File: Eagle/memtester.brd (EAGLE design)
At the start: 69 x 22.3 mm, 15 parts, among them IC1 HT7833, J3 SM08B-SRSS-TB(LF)(SN), U1 ATTINY1616-MFR

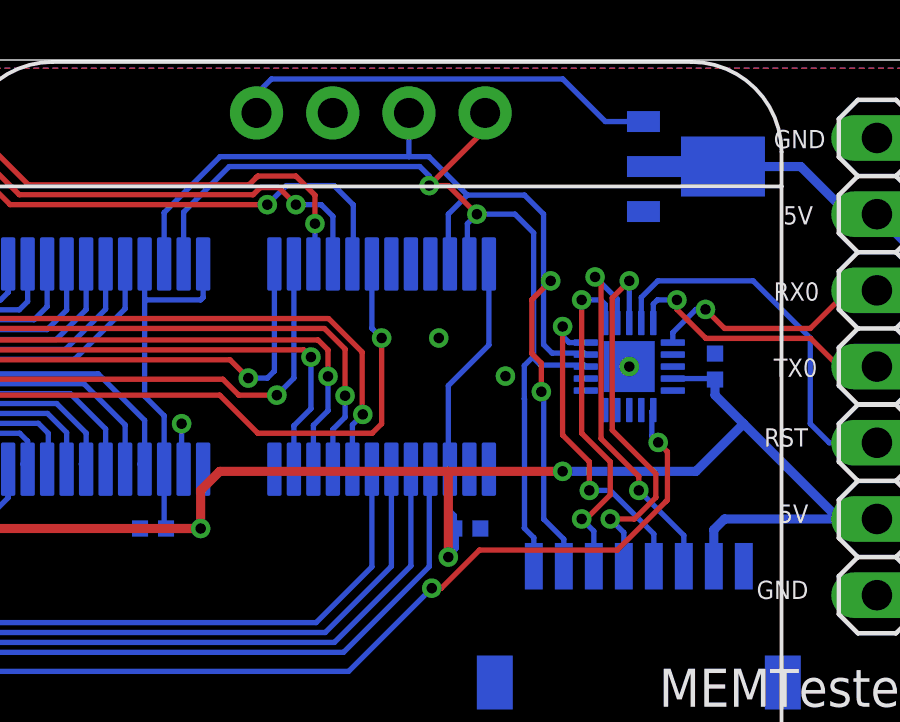
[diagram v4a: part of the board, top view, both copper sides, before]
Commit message: Memtester: i2c pull-ups, labels, credits
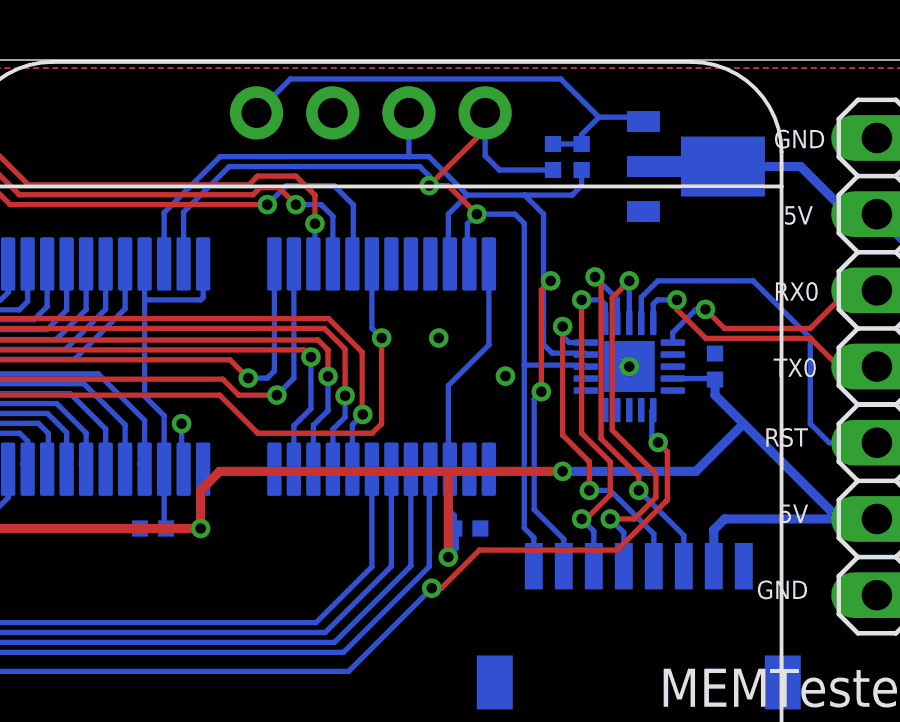
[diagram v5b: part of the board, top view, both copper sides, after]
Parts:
- added R1, R2: 4k7, passives:0402_RES
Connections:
- removed net N$1: IC1.1, U$6.VCC
- new net +3V3: IC1.1, R1.1, R2.1, U$6.VCC
- net I2C_SCL: now also R2.2
- net I2C_SDA: now also R1.2
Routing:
- net +3V3: track 0.00 -> 16.2 mm
- net N$1: track 14.3 -> 0.00 mm
- net I2C_SDA: track 33.4 -> 37.2 mm
- net I2C_SCL: track 36.4 -> 38.8 mm
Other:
- board text added: "Petrkr.NET"
- board text added: "Version 1 (2023/05)"
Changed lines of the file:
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@@
 <drawing>
 <settings>
-<setting alwaysvectorfont="yes"/>
+<setting alwaysvectorfont="no"/>
 <setting verticaltext="up"/>
 </settings>
@@
 <text x="60.96" y="6.985" size="0.6096" layer="26" rot="MR270" align="center-right">5V</text>
 <text x="61.9125" y="6.985" size="0.6096" layer="26" rot="MR270" align="center-right">GND</text>
+<text x="51.1175" y="0.635" size="0.8128" layer="26" rot="MR0">Version 1 (2023/05)</text>
+<text x="51.1175" y="2.2225" size="1.0668" layer="26" rot="MR0">Petrkr.NET</text>
 </plain>
 <attributes>
@@
 <element name="IC1" library="holtek2" package="SOT-89" value="HT7833" x="60.96" y="18.7325" smashed="yes" rot="MR90">
 <attribute name="LCSC_PART" value="C50936" x="69.85" y="11.1125" size="1.778" layer="28" rot="MR90" display="off"/>
-<attribute name="NAME" x="55.795" y="17.7975" size="1.27" layer="26" rot="MR90"/>
+<attribute name="NAME" x="61.8275" y="14.94" size="1.27" layer="26" rot="MR0"/>
 </element>
 <element name="C4" library="passives" package="0402_CAP" value="100nF" x="60.96" y="12.065" smashed="yes" rot="MR90">
-<attribute name="NAME" x="59.436" y="12.065" size="0.635" layer="26" font="vector" ratio="12" rot="MR90" align="bottom-center"/>
+<attribute name="NAME" x="60.706" y="10.4775" size="0.635" layer="26" font="vector" ratio="12" rot="MR90" align="bottom-center"/>
+</element>
+<element name="R2" library="passives" package="0402_RES" value="4k7" x="56.515" y="19.05" smashed="yes" rot="MR270">
+<attribute name="NAME" x="56.769" y="20.6375" size="0.635" layer="26" font="vector" ratio="12" rot="MR270" align="bottom-center"/>
+</element>
+<element name="R1" library="passives" package="0402_RES" value="4k7" x="55.5625" y="19.05" smashed="yes" rot="MR270">
+<attribute name="NAME" x="55.8165" y="20.6375" size="0.635" layer="26" font="vector" ratio="12" rot="MR270" align="bottom-center"/>
 </element>
 </elements>
@@
 <contactref element="U1" pad="13"/>
 <wire x1="56.6525" y1="12.065" x2="56.6038" y2="12.1137" width="0.1778" layer="16"/>
-<wire x1="56.6038" y1="12.1137" x2="55.1441875" y2="12.1137" width="0.1778" layer="16"/>
+<wire x1="56.6038" y1="12.1137" x2="54.61813125" y2="12.1137" width="0.1778" layer="16"/>
 <wire x1="52.705" y1="15.5525" x2="52.705" y2="16.8275" width="0.1778" layer="16"/>
 <wire x1="52.705" y1="15.5525" x2="52.7725" y2="15.485" width="0.1778" layer="16"/>
@@
 <wire x1="52.07" y1="18.0975" x2="51.435" y2="18.0975" width="0.1778" layer="1"/>
 <via x="53.0225" y="17.145" extent="1-16" drill="0.35"/>
-<wire x1="54.9148" y1="16.5227" x2="54.2925" y2="17.145" width="0.1778" layer="16"/>
+<wire x1="54.6025" y1="16.835" x2="54.2925" y2="17.145" width="0.1778" layer="16"/>
 <wire x1="53.0225" y1="17.145" x2="54.2925" y2="17.145" width="0.1778" layer="16"/>
-<wire x1="54.9148" y1="16.5227" x2="54.9148" y2="12.41036875" width="0.1778" layer="16"/>
+<wire x1="54.6025" y1="16.835" x2="54.6025" y2="12.09806875" width="0.1778" layer="16"/>
 <wire x1="52.705" y1="16.8275" x2="53.0225" y2="17.145" width="0.1778" layer="16"/>
 <contactref element="U$6" pad="SDA"/>
@@
 <wire x1="54.92" y1="5.41" x2="54.92" y2="6.3625" width="0.1778" layer="16"/>
 <wire x1="54.6025" y1="6.68" x2="54.92" y2="6.3625" width="0.1778" layer="16"/>
-<wire x1="54.9148" y1="12.41036875" x2="54.6025" y2="12.09806875" width="0.1778" layer="16"/>
-<wire x1="54.6025" y1="12.09806875" x2="54.6025" y2="10.99193125" width="0.1778" layer="16"/>
-<wire x1="54.6025" y1="10.99193125" x2="54.61" y2="10.98443125" width="0.1778" layer="16"/>
-<wire x1="54.61" y1="6.6875" x2="54.6025" y2="6.68" width="0.1778" layer="16"/>
-<wire x1="54.61" y1="10.98443125" x2="54.61" y2="6.6875" width="0.1778" layer="16"/>
-<wire x1="54.9148" y1="12.3430875" x2="54.9148" y2="12.41036875" width="0.1778" layer="16"/>
-<wire x1="55.1441875" y1="12.1137" x2="54.9148" y2="12.3430875" width="0.1778" layer="16"/>
+<wire x1="54.61813125" y1="12.1137" x2="54.6025" y2="12.09806875" width="0.1778" layer="16"/>
+<wire x1="54.6025" y1="12.09806875" x2="54.6025" y2="6.68" width="0.1778" layer="16"/>
+<contactref element="R1" pad="2"/>
+<wire x1="55.5625" y1="18.61693125" x2="53.77306875" y2="18.61693125" width="0.1778" layer="16"/>
+<wire x1="53.2975" y1="19.0925" x2="53.2975" y2="20.52" width="0.1778" layer="16"/>
+<wire x1="53.77306875" y1="18.61693125" x2="53.2975" y2="19.0925" width="0.1778" layer="16"/>
 </signal>
 <signal name="I2C_SCL">
@@
 <contactref element="J3" pad="7"/>
 <wire x1="55.92" y1="5.41" x2="55.92" y2="6.31" width="0.1778" layer="16"/>
-<wire x1="55.2502" y1="6.9798" x2="55.2502" y2="11.2275" width="0.1778" layer="16"/>
-<wire x1="55.2502" y1="11.2275" x2="55.1712" y2="11.2275" width="0.1778" layer="16"/>
+<wire x1="55.1712" y1="11.2275" x2="54.9327" y2="10.989" width="0.1778" layer="16"/>
+<wire x1="54.9327" y1="10.989" x2="54.9327" y2="7.2973" width="0.1778" layer="16"/>
 <via x="55.1712" y="11.2275" extent="1-16" drill="0.35"/>
-<wire x1="54.8537" y1="12.4975" x2="54.8536875" y2="14.2926875" width="0.1778" layer="1"/>
-<wire x1="55.4835" y1="14.9225" x2="54.8536875" y2="14.2926875" width="0.1778" layer="1"/>
-<wire x1="55.1712" y1="11.2275" x2="55.1712" y2="12.18" width="0.1778" layer="1"/>
-<wire x1="55.1712" y1="12.18" x2="54.8537" y2="12.4975" width="0.1778" layer="1"/>
+<wire x1="55.1712" y1="11.2275" x2="55.17118125" y2="14.61018125" width="0.1778" layer="1"/>
+<wire x1="55.4835" y1="14.9225" x2="55.17118125" y2="14.61018125" width="0.1778" layer="1"/>
 <via x="55.4835" y="14.9225" extent="1-16" drill="0.35"/>
 <wire x1="55.4835" y1="14.9225" x2="55.245" y2="14.9225" width="0.1778" layer="16"/>
-<wire x1="55.92" y1="6.31" x2="55.2502" y2="6.9798" width="0.1778" layer="16"/>
+<wire x1="55.92" y1="6.31" x2="54.9327" y2="7.2973" width="0.1778" layer="16"/>
+<contactref element="R2" pad="2"/>
+<wire x1="56.515" y1="18.61693125" x2="56.515" y2="18.0975" width="0.1778" layer="16"/>
+<wire x1="56.515" y1="18.0975" x2="56.1975" y2="17.78" width="0.1778" layer="16"/>
+<wire x1="56.1975" y1="17.78" x2="54.61" y2="17.78" width="0.1778" layer="16"/>
 </signal>
 <signal name="OE">
@@
 <wire x1="57.4675" y1="7.78926875" x2="57.4675" y2="8.89" width="0.1778" layer="1"/>
 </signal>
-<signal name="N$1">
+<signal name="+3V3">
+<contactref element="R2" pad="1"/>
+<contactref element="R1" pad="1"/>
 <contactref element="IC1" pad="1"/>
 <contactref element="U$6" pad="VCC"/>
-<wire x1="45.6775" y1="20.52" x2="45.6775" y2="21.155" width="0.1778" layer="16"/>
-<wire x1="46.1728" y1="21.6503" x2="45.6775" y2="21.155" width="0.1778" layer="16"/>
-<wire x1="46.1728" y1="21.6503" x2="55.8872" y2="21.6503" width="0.1778" layer="16"/>
-<wire x1="57.305" y1="20.2325" x2="55.8872" y2="21.6503" width="0.1778" layer="16"/>
-<wire x1="57.305" y1="20.2325" x2="58.575" y2="20.2325" width="0.1778" layer="16"/>
+<wire x1="45.6775" y1="20.52" x2="46.8078" y2="21.6503" width="0.1778" layer="16"/>
+<wire x1="58.4875" y1="20.32" x2="58.575" y2="20.2325" width="0.1778" layer="16"/>
+<wire x1="46.8078" y1="21.6503" x2="55.8197" y2="21.6503" width="0.1778" layer="16"/>
+<wire x1="55.8197" y1="21.6503" x2="57.092215625" y2="20.377784375" width="0.1778" layer="16"/>
+<wire x1="55.5625" y1="19.48306875" x2="56.515" y2="19.48306875" width="0.1778" layer="16"/>
+<wire x1="56.515" y1="19.80056875" x2="57.092215625" y2="20.377784375" width="0.1778" layer="16"/>
+<wire x1="56.515" y1="19.48306875" x2="56.515" y2="19.80056875" width="0.1778" layer="16"/>
+<wire x1="57.092215625" y1="20.377784375" x2="58.429715625" y2="20.377784375" width="0.1778" layer="16"/>
+<wire x1="58.429715625" y1="20.377784375" x2="58.575" y2="20.2325" width="0.1778" layer="16"/>
 </signal>
 </signals>

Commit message: Memtester: leds, button
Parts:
- added LED1, LED2: green, led:CHIP-LED0805
- added R3, R4: 2k, passives:0402_RES
- added SW1: BTN, SparkFun-Switches:TACTILE_SWITCH_SMD_6.0X3.5MM
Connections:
- new net N$2: LED1.C, R3.1
- new net N$3: LED2.C, R4.1
- net GND: now also R3.2, R4.2, SW1.2
- net PB2: now also SW1.1
- net PB4: now also LED1.A
- net PB5: now also LED2.A
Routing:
- net PB4: track 0.00 -> 44.3 mm, vias 0 -> 1
- net PB5: track 0.00 -> 36.9 mm, vias 0 -> 1
- net PB2: track 0.00 -> 20.7 mm, vias 0 -> 2
- net N$2: track 0.00 -> 2.01 mm, vias 0 -> 1
- net N$3: track 0.00 -> 2.01 mm, vias 0 -> 1
- net +5V: track 143.0 -> 144.0 mm
- net RAS0: track 45.7 -> 46.2 mm
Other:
- board text added: "3v3"

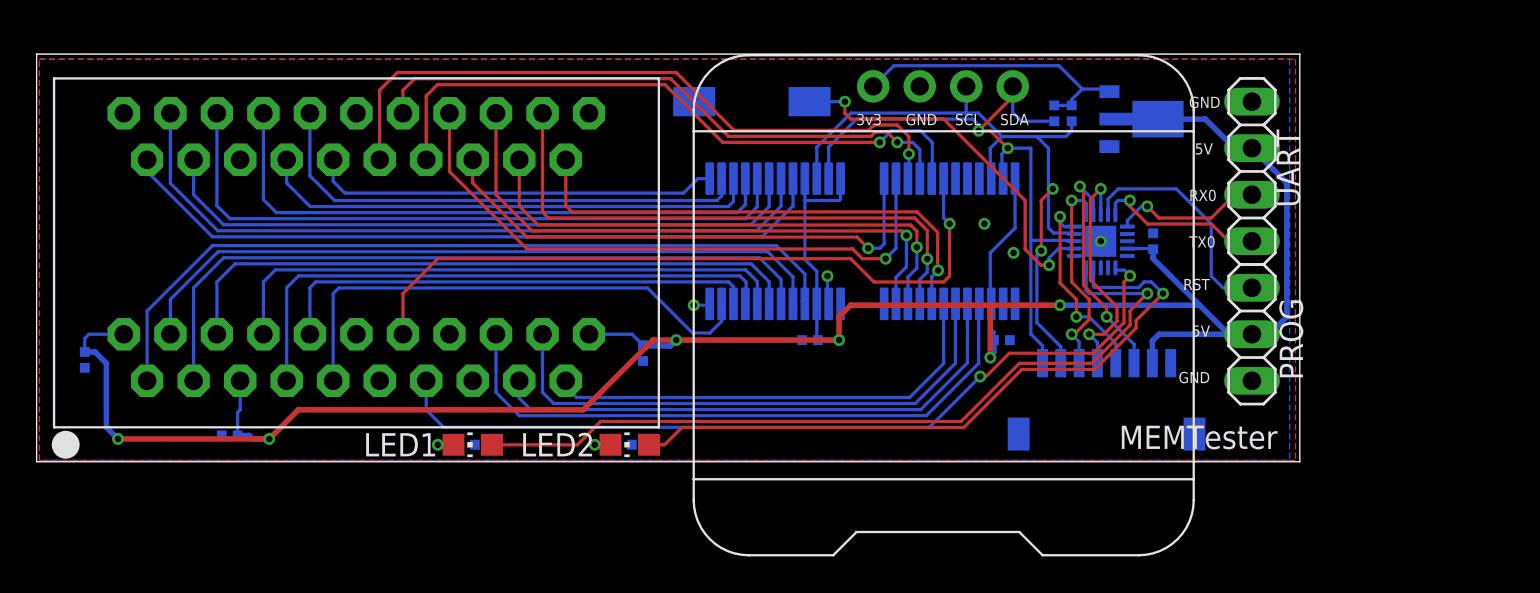
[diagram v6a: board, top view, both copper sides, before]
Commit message: Memtester: Labels, wirestubs
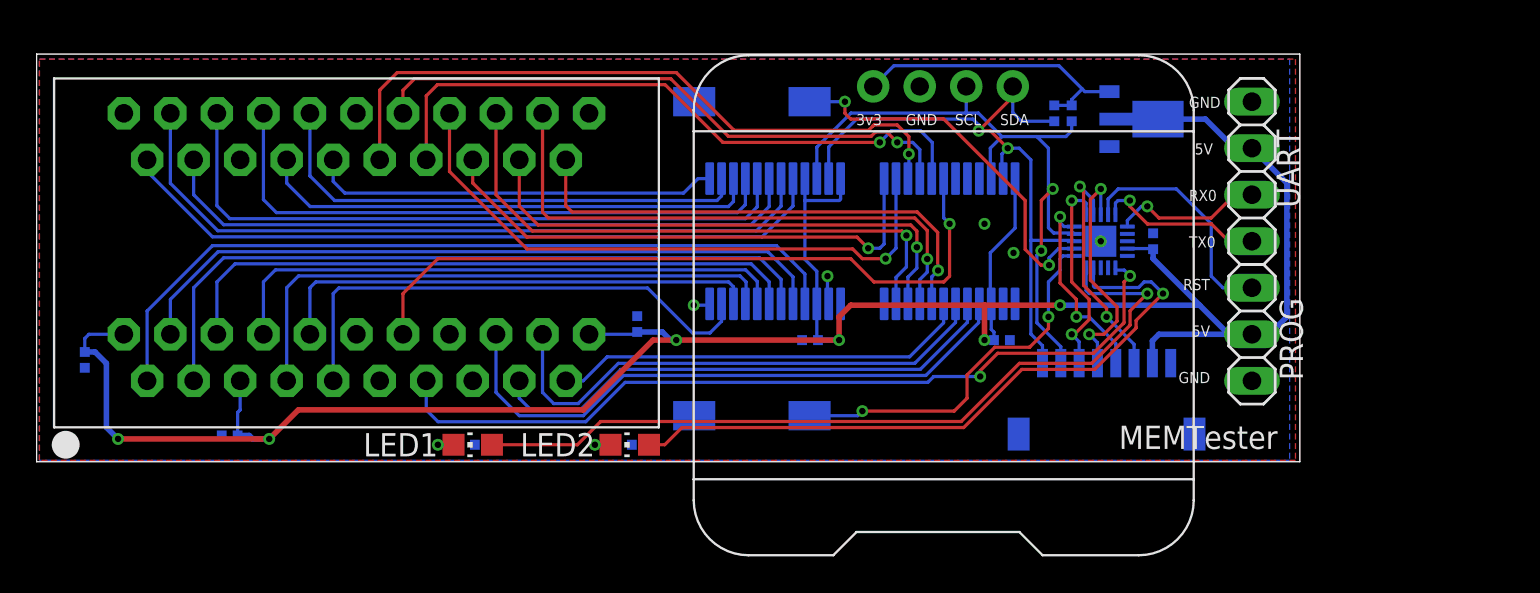
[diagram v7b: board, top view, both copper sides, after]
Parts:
- added SW2: BTN, SparkFun-Switches:TACTILE_SWITCH_SMD_6.0X3.5MM
- moved C2 1.62 mm to (32.8, 7.54), turned to 270 degrees
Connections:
- net GND: now also SW2.2
- net PB3: now also SW2.1
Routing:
- net PB3: track 0.00 -> 20.7 mm, vias 0 -> 2
- net A3: track 25.2 -> 23.0 mm
- net +5V: track 144.0 -> 141.7 mm
- net A2: track 30.1 -> 28.8 mm
- net A1: track 30.0 -> 28.7 mm
- net A0: track 34.5 -> 33.2 mm
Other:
- board text added: "PA0 - UPDI PA5 - RAS"
- board text added: "PA1 - TXD PA2 - RXD PB0 - SCL PB1 - SDA"
- board text added: "PB2 - SW1 PB3 - SW2 PB4 - LED1 PB5 - LED2"
- board text added: "PC0 - SCLK PC1 - MISO PC2 - MOSI PC3 - CS"

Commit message: Memtester: C values
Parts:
- C1, C2, C3: value (none) -> 100n
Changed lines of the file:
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@@
 </autorouter>
 <elements>
-<element name="C1" library="passives" package="0402_CAP" value="" x="2.6289" y="5.586428125" smashed="yes" rot="MR90">
+<element name="C1" library="passives" package="0402_CAP" value="100n" x="2.6289" y="5.586428125" smashed="yes" rot="MR90">
 <attribute name="NAME" x="3.3274" y="5.586428125" size="0.635" layer="26" font="vector" rot="MR90" align="bottom-center"/>
 </element>
-<element name="C2" library="passives" package="0402_CAP" value="" x="32.7914" y="7.543071875" smashed="yes" rot="MR270">
+<element name="C2" library="passives" package="0402_CAP" value="100n" x="32.7914" y="7.543071875" smashed="yes" rot="MR270">
 <attribute name="NAME" x="34.0609" y="7.924071875" size="0.635" layer="26" font="vector" rot="MR270"/>
 <attribute name="VALUE" x="35.3314" y="8.813071875" size="1.27" layer="28" rot="MR270"/>
 </element>
-<element name="C3" library="passives" package="0402_CAP" value="" x="10.541" y="1.458971875" smashed="yes" rot="MR180">
+<element name="C3" library="passives" package="0402_CAP" value="100n" x="10.541" y="1.458971875" smashed="yes" rot="MR180">
 <attribute name="NAME" x="10.1405" y="2.795471875" size="0.635" layer="26" font="vector" rot="MR180"/>
 <attribute name="VALUE" x="9.271" y="3.998971875" size="1.27" layer="28" rot="MR180"/>
